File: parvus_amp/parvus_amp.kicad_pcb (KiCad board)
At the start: 2 copper layers, 86 x 60 mm, 43 parts, among them J1 input, J2 output, J3 powersupply, U1 LM3886

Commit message: WIP: Component placement.
Signed-off-by: Nenad Radulovic <nenad.b.radulovic@gmail.com>
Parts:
- removed R14: 7k5, Resistor_THT:R_Axial_DIN0207_L6.3mm_D2.5mm_P7.62mm_Horizontal
- added D4: BZX85C15, Diode_THT:D_DO-41_SOD81_P10.16mm_Horizontal, F.Cu at (115.4, 86.3)
- added J4: ctrl, Connector_PinHeader_2.54mm:PinHeader_1x04_P2.54mm_Vertical, F.Cu at (118.0, 90.1)
- C1: value 15p -> 2m2; footprint Capacitor_THT:C_Disc_D3.8mm_W2.6mm_P2.50mm -> Capacitor_THT:CP_Radial_D16.0mm_P7.50mm
- C10: value 2m2 -> 3p3; footprint Capacitor_THT:CP_Radial_D16.0mm_P7.50mm -> Capacitor_THT:C_Disc_D3.8mm_W2.6mm_P2.50mm
- C11: value 100n -> 47u; footprint Capacitor_THT:C_Rect_L7.0mm_W3.5mm_P5.00mm -> Capacitor_THT:CP_Radial_D6.3mm_P2.50mm
- C12: value 100u -> 10u; footprint Capacitor_THT:CP_Radial_D8.0mm_P3.50mm -> Capacitor_THT:CP_Radial_D5.0mm_P2.00mm
- C13: value 2m2 -> 100n; footprint Capacitor_THT:CP_Radial_D16.0mm_P7.50mm -> Capacitor_THT:C_Rect_L4.6mm_W3.0mm_P2.50mm_MKS02_FKP02
- C14: value 100n -> 10u; footprint Capacitor_THT:C_Rect_L7.0mm_W3.5mm_P5.00mm -> Capacitor_THT:CP_Radial_D5.0mm_P2.00mm
- C15: value 100u -> 100n; footprint Capacitor_THT:CP_Radial_D8.0mm_P3.50mm -> Capacitor_THT:C_Disc_D5.1mm_W3.2mm_P5.00mm
- C2: value 220n -> 2m2; footprint Capacitor_THT:C_Rect_L7.0mm_W3.5mm_P5.00mm -> Capacitor_THT:CP_Radial_D16.0mm_P7.50mm
- C3: value 100n -> 220n; footprint Capacitor_THT:C_Rect_L7.0mm_W3.5mm_P5.00mm -> Capacitor_THT:C_Rect_L4.6mm_W3.0mm_P2.50mm_MKS02_FKP02
- C4: value 470u -> 220n; footprint Capacitor_THT:CP_Radial_D8.0mm_P3.50mm -> Capacitor_THT:C_Rect_L4.6mm_W3.0mm_P2.50mm_MKS02_FKP02
- C5: value 220p -> 22n; footprint Capacitor_THT:C_Disc_D4.3mm_W1.9mm_P5.00mm -> Capacitor_THT:C_Rect_L4.6mm_W3.0mm_P2.50mm_MKS02_FKP02
- C6: value 1n -> 22n; footprint Capacitor_THT:C_Disc_D4.3mm_W1.9mm_P5.00mm -> Capacitor_THT:C_Rect_L4.6mm_W3.0mm_P2.50mm_MKS02_FKP02
- C7: value 470u -> 10u; footprint Capacitor_THT:CP_Radial_D8.0mm_P3.50mm -> Capacitor_THT:CP_Radial_D5.0mm_P2.00mm
- C8: value 15p -> 220u; footprint Capacitor_THT:C_Disc_D3.8mm_W2.6mm_P2.50mm -> Capacitor_THT:CP_Radial_D6.3mm_P2.50mm
- C9: value 100u -> 3p3; footprint Capacitor_THT:CP_Radial_D8.0mm_P3.50mm -> Capacitor_THT:C_Disc_D3.8mm_W2.6mm_P2.50mm
- D1, D2: footprint Diode_THT:D_DO-201AD_P12.70mm_Horizontal -> Diode_THT:D_DO-35_SOD27_P7.62mm_Horizontal
- D3: value BZX85C16 -> 1N4148
- J1: footprint TerminalBlock_Phoenix:TerminalBlock_Phoenix_PT-1,5-3-3.5-H_1x03_P3.50mm_Horizontal -> Connector_Phoenix_MC:PhoenixContact_MCV_1,5_3-G-3.5_1x03_P3.50mm_Vertical
- J2: value output -> power; footprint Connector_Phoenix_MC:PhoenixContact_MCV_1,5_2-G-3.5_1x02_P3.50mm_Vertical -> Connector_Phoenix_MC:PhoenixContact_MCV_1,5_3-G-3.81_1x03_P3.81mm_Vertical
- J3: value powersupply -> output; footprint Connector_Phoenix_MC:PhoenixContact_MCV_1,5_3-G-3.5_1x03_P3.50mm_Vertical -> Connector_Phoenix_MC:PhoenixContact_MCV_1,5_2-G-3.81_1x02_P3.81mm_Vertical
- L1: value 2u -> 4u; footprint Inductor_THT:L_Axial_L12.0mm_D5.0mm_P15.24mm_Horizontal_Fastron_MISC -> Inductor_THT:L_Axial_L20.3mm_D12.7mm_P7.62mm_Vertical_Vishay_IHA-201
- R1: value 1k6 -> 499; footprint Resistor_THT:R_Axial_DIN0207_L6.3mm_D2.5mm_P7.62mm_Horizontal -> Resistor_THT:R_Axial_DIN0207_L6.3mm_D2.5mm_P10.16mm_Horizontal
- R10: value 499 -> 10
- R11: value 7k5 -> 47k; footprint Resistor_THT:R_Axial_DIN0207_L6.3mm_D2.5mm_P10.16mm_Horizontal -> Resistor_THT:R_Axial_DIN0204_L3.6mm_D1.6mm_P5.08mm_Horizontal
- R12: value 10 -> 30k; footprint Resistor_THT:R_Axial_DIN0207_L6.3mm_D2.5mm_P10.16mm_Horizontal -> Resistor_THT:R_Axial_DIN0204_L3.6mm_D1.6mm_P5.08mm_Horizontal
- R13: value 1k6 -> 10k; footprint Resistor_THT:R_Axial_DIN0207_L6.3mm_D2.5mm_P7.62mm_Horizontal -> Resistor_THT:R_Axial_DIN0204_L3.6mm_D1.6mm_P5.08mm_Horizontal
- R2: value 4.7 -> 499; footprint Resistor_THT:R_Axial_DIN0411_L9.9mm_D3.6mm_P15.24mm_Horizontal -> Resistor_THT:R_Axial_DIN0207_L6.3mm_D2.5mm_P10.16mm_Horizontal
- R3: value 10 -> 499
- R4: value 100 -> 499; footprint Resistor_THT:R_Axial_DIN0207_L6.3mm_D2.5mm_P7.62mm_Horizontal -> Resistor_THT:R_Axial_DIN0207_L6.3mm_D2.5mm_P10.16mm_Horizontal
- R5: value 100 -> 12k; footprint Resistor_THT:R_Axial_DIN0207_L6.3mm_D2.5mm_P7.62mm_Horizontal -> Resistor_THT:R_Axial_DIN0207_L6.3mm_D2.5mm_P10.16mm_Horizontal
- R6: value 499 -> 12k
- R7: value 7k5 -> 3.9
- R8: value 100k -> 15k; footprint Resistor_THT:R_Axial_DIN0207_L6.3mm_D2.5mm_P7.62mm_Horizontal -> Resistor_THT:R_Axial_DIN0204_L3.6mm_D1.6mm_P5.08mm_Horizontal
- R9: value 4.7 -> 3.9; footprint Resistor_THT:R_Axial_DIN0411_L9.9mm_D3.6mm_P15.24mm_Horizontal -> Resistor_THT:R_Axial_DIN0207_L6.3mm_D2.5mm_P10.16mm_Horizontal
- U1: value LM3886 -> TDA7293; footprint Package_TO_SOT_THT:TO-220-11_P3.4x5.08mm_StaggerOdd_Lead4.85mm_Vertical -> Package_TO_SOT_THT:TO-220-15_P2.54x2.54mm_StaggerOdd_Lead4.58mm_Vertical
- moved C8 67.9 mm to (99.6, 68.5), turned to 180 degrees
- moved C7 65.1 mm to (99.6, 76.1), turned to 180 degrees
- moved J1 62.1 mm to (97.0, 94.5)
- moved R3 54.5 mm to (114.2, 67.9), turned to 180 degrees
- moved C13 53.2 mm to (144.6, 66.0), turned to 270 degrees
- moved D1 50.4 mm to (151.0, 55.8), turned to 270 degrees
- moved C15 49.1 mm to (159.2, 90.7), turned to 270 degrees
- moved R1 48.5 mm to (104.0, 80.6)
- moved R12 48.1 mm to (120.5, 72.9)
- moved D2 46.9 mm to (147.8, 63.4), turned to 90 degrees
- moved R4 46.5 mm to (114.2, 64.7), turned to 180 degrees
- moved R8 44.4 mm to (120.5, 78.0)
- moved R5 43.4 mm to (114.2, 74.2), turned to 180 degrees
- moved C3 41.5 mm to (129.4, 66.0)
- moved J3 40.4 mm to (150.4, 94.5)
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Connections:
- C1 pad 1: Net-(C1-Pad1) -> +pwvs
- C1 pad 2: Net-(C1-Pad2) -> GNDD
- C10 pad 1: VCC -> Net-(C10-Pad1)
- C10 pad 2: GNDPWR -> /preout
- C11 pad 1: VCC -> Net-(C11-Pad1)
- C11 pad 2: GNDPWR -> /preout
- C12 pad 1: VCC -> Net-(C12-Pad1)
- C12 pad 2: GNDPWR -> GNDD
- C13 pad 1: GNDPWR -> Net-(C13-Pad1)
- C13 pad 2: VEE -> GNDD
- C14 pad 1: GNDPWR -> Net-(C14-Pad1)
- C14 pad 2: VEE -> GNDD
- C15 pad 1: GNDPWR -> Net-(C15-Pad1)
- C15 pad 2: VEE -> GNDD
- C2 pad 1: Net-(C2-Pad1) -> GNDD
- C2 pad 2: Net-(C2-Pad2) -> -pwvs
- C3 pad 1: Net-(C3-Pad1) -> +pwvs
- C3 pad 2: Net-(C3-Pad2) -> GNDD
- C4 pad 1: Net-(C4-Pad1) -> GNDD
- C4 pad 2: Net-(C4-Pad2) -> -pwvs
- C5 pad 1: Net-(C5-Pad1) -> +pwvs
- C5 pad 2: Net-(C1-Pad1) -> GNDD
- C6 pad 1: Net-(C4-Pad2) -> GNDD
- C6 pad 2: Net-(C1-Pad1) -> -pwvs
- C7 pad 2: Net-(C1-Pad1) -> /input
- C8 pad 1: Net-(C2-Pad2) -> Net-(C8-Pad1)
- C8 pad 2: Net-(C8-Pad2) -> /sgnd
- C9 pad 1: GNDPWR -> /sgnd
- D1 pad 1: VCC -> +pwvs
- D1 pad 2: Net-(C2-Pad2) -> /preout
- D2 pad 1: Net-(C2-Pad2) -> /preout
- D2 pad 2: VEE -> -pwvs
- D3 pad 2: Net-(C9-Pad2) -> Net-(D3-Pad2)
- J1 pad 1: Net-(J1-Pad1) -> /input
- J1 pad 2: GNDPWR -> /sgnd
- J1 pad 3: Net-(C1-Pad1) -> GNDD
- J2 pad 1: GNDPWR -> +pwvs
- J2 pad 2: Net-(C3-Pad2) -> GNDD
- J3 pad 1: VCC -> /out
- J3 pad 2: GNDPWR -> GNDD
- L1 pad 1: Net-(C2-Pad2) -> /preout
- L1 pad 2: Net-(C3-Pad2) -> /out
- R1 pad 1: Net-(R1-Pad1) -> /sgnd
- R1 pad 2: Net-(C1-Pad2) -> /input
- R10 pad 1: Net-(R10-Pad1) -> /out
- R10 pad 2: Net-(C7-Pad1) -> Net-(C15-Pad1)
- R11 pad 1: Net-(C2-Pad2) -> Net-(D3-Pad1)
- R11 pad 2: Net-(R10-Pad1) -> Net-(D3-Pad2)
- R12 pad 1: Net-(C1-Pad1) -> Net-(D3-Pad1)
- R12 pad 2: GNDPWR -> Net-(C14-Pad1)
- R13 pad 1: Net-(R10-Pad1) -> GNDD
- R13 pad 2: Net-(C8-Pad2) -> Net-(D3-Pad1)
- R2 pad 1: GNDPWR -> GNDD
- R2 pad 2: Net-(C2-Pad1) -> /sgnd
- R3 pad 1: GNDPWR -> Net-(C9-Pad2)
- R3 pad 2: Net-(C3-Pad1) -> Net-(C7-Pad1)
- R4 pad 1: Net-(C5-Pad1) -> Net-(C10-Pad1)
- R4 pad 2: Net-(J1-Pad1) -> Net-(C8-Pad1)
- R5 pad 1: Net-(C4-Pad2) -> Net-(C9-Pad2)
- R5 pad 2: Net-(C5-Pad1) -> /sgnd
- R6 pad 1: Net-(R1-Pad1) -> Net-(C10-Pad1)
- R6 pad 2: Net-(C4-Pad1) -> /preout
- R7 pad 1: Net-(C1-Pad1) -> /preout
- R7 pad 2: Net-(R1-Pad1) -> Net-(C13-Pad1)
- R8 pad 1: Net-(J1-Pad1) -> Net-(D3-Pad2)
- R8 pad 2: Net-(C1-Pad1) -> Net-(C12-Pad1)
- R9 pad 1: Net-(C3-Pad2) -> /out
- R9 pad 2: Net-(C2-Pad2) -> /preout
- U1 pad 1: VCC -> GNDD
- U1 pad 10: Net-(R1-Pad1) -> Net-(C12-Pad1)
- U1 pad 2: (no net) -> Net-(C10-Pad1)
- U1 pad 3: Net-(C2-Pad2) -> Net-(C9-Pad2)
- U1 pad 4: VEE -> /sgnd
- U1 pad 5: VCC -> Net-(J4-Pad4)
- U1 pad 6: (no net) -> Net-(C11-Pad1)
- U1 pad 7: GNDPWR -> +pwvs
- U1 pad 8: Net-(D3-Pad1) -> -pwvs
- U1 pad 9: Net-(R10-Pad1) -> Net-(C14-Pad1)
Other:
- board size 86 x 60 mm -> 70 x 54.9 mm

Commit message: WIP: Routing components
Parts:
- removed the C11 at (140.8, 58.3)
- removed the C13 at (144.6, 66.0)
- removed the C15 at (159.2, 90.7)
- removed the C2 at (135.1, 78.7)
- removed C3: 220n, Capacitor_THT:C_Rect_L4.6mm_W3.0mm_P2.50mm_MKS02_FKP02
- removed the C7 at (99.6, 76.1)
- removed the D1 at (151.0, 55.8)
- removed the J4 at (118.0, 90.1)
- removed the R10 at (149.1, 88.2)
- removed the R13 at (120.5, 75.5)
- removed R8: 15k, Resistor_THT:R_Axial_DIN0204_L3.6mm_D1.6mm_P5.08mm_Horizontal
- added C10: 100n, Capacitor_THT:C_Disc_D5.1mm_W3.2mm_P5.00mm, F.Cu at (104.0, 89.5)
- added C12: 220n, Capacitor_THT:C_Rect_L4.6mm_W3.0mm_P2.50mm_MKS02_FKP02, F.Cu at (129.4, 66.0)
- added C14: 2m2, Capacitor_THT:CP_Radial_D16.0mm_P7.50mm, F.Cu at (133.3, 78.8)
- added C4: 47u, Capacitor_THT:CP_Radial_D6.3mm_P2.50mm, F.Cu at (143.0, 57.4)
- added C5: 220p, Capacitor_THT:C_Disc_D3.8mm_W2.6mm_P2.50mm, F.Cu at (114.2, 75.6)
- added C6: 3u3, Capacitor_THT:CP_Radial_D5.0mm_P2.00mm, F.Cu at (107.2, 72.4)
- added D3: 1N5404, Diode_THT:D_DO-201AD_P12.70mm_Horizontal, F.Cu at (158.5, 66.0)
- added J2: input, Connector_Phoenix_MC:PhoenixContact_MCV_1,5_3-G-3.5_1x03_P3.50mm_Vertical, F.Cu at (97.7, 80.6)
- added R14: 10, Resistor_THT:R_Axial_DIN0207_L6.3mm_D2.5mm_P10.16mm_Horizontal, F.Cu at (114.2, 93.3)
- added R4: 10k, Resistor_THT:R_Axial_DIN0207_L6.3mm_D2.5mm_P10.16mm_Horizontal, F.Cu at (127.5, 85.7)
- added R7: 12k, Resistor_THT:R_Axial_DIN0207_L6.3mm_D2.5mm_P10.16mm_Horizontal, F.Cu at (114.2, 81.9)
- C7: renamed from C8; value 220u -> 470u
- C9: value 3p3 -> 100n; footprint Capacitor_THT:C_Disc_D3.8mm_W2.6mm_P2.50mm -> Capacitor_THT:C_Rect_L4.6mm_W3.0mm_P2.50mm_MKS02_FKP02
- D2: value 1N5404 -> BZX79C15
- D4: value BZX85C15 -> 1N5404; footprint Diode_THT:D_DO-41_SOD81_P10.16mm_Horizontal -> Diode_THT:D_DO-201AD_P12.70mm_Horizontal
- J1: value input -> ctrl; footprint Connector_Phoenix_MC:PhoenixContact_MCV_1,5_3-G-3.5_1x03_P3.50mm_Vertical -> Connector_PinHeader_2.54mm:PinHeader_1x04_P2.54mm_Vertical
- R1: value 499 -> 15k; footprint Resistor_THT:R_Axial_DIN0207_L6.3mm_D2.5mm_P10.16mm_Horizontal -> Resistor_THT:R_Axial_DIN0204_L3.6mm_D1.6mm_P7.62mm_Horizontal
- R11: value 47k -> 10; footprint Resistor_THT:R_Axial_DIN0204_L3.6mm_D1.6mm_P5.08mm_Horizontal -> Resistor_THT:R_Axial_DIN0207_L6.3mm_D2.5mm_P10.16mm_Horizontal
- R12: value 30k -> 12k; footprint Resistor_THT:R_Axial_DIN0204_L3.6mm_D1.6mm_P5.08mm_Horizontal -> Resistor_THT:R_Axial_DIN0207_L6.3mm_D2.5mm_P10.16mm_Horizontal
- R2: value 499 -> 47k; footprint Resistor_THT:R_Axial_DIN0207_L6.3mm_D2.5mm_P10.16mm_Horizontal -> Resistor_THT:R_Axial_DIN0204_L3.6mm_D1.6mm_P7.62mm_Horizontal
- R3: value 499 -> 30k; footprint Resistor_THT:R_Axial_DIN0207_L6.3mm_D2.5mm_P10.16mm_Horizontal -> Resistor_THT:R_Axial_DIN0204_L3.6mm_D1.6mm_P7.62mm_Horizontal
- R6: value 12k -> 100
- moved LOGO1 78.9 mm to (137.0, 104.1)
- moved J3 44.7 mm to (105.9, 99.7)
- moved D4 38.2 mm to (152.9, 78.7), turned to 90 degrees
- moved C9 33.1 mm to (144.6, 68.6), turned to 90 degrees
- moved D2 29.8 mm to (125.0, 82.5), turned to 180 degrees
- moved R11 22.1 mm to (104.0, 85.1), turned to 0 degrees
- moved LOGO2 22.0 mm to (148.5, 102.4)
- moved J1 20.9 mm to (117.3, 89.5), turned to 90 degrees
- moved R6 20.4 mm to (114.2, 78.7)
- moved R12 15.9 mm to (114.2, 58.4), turned to 180 degrees
- moved R1 14.5 mm to (117.3, 74.9)
- moved L1 13.4 mm to (154.8, 87.6), turned to 180 degrees
- moved R5 11.9 mm to (104.0, 67.9), turned to 0 degrees
- moved R9 11.0 mm to (147.2, 95.9)
- moved R13 10.8 mm to (148.5, 66.0), turned to 270 degrees
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- renumbered C12 to C1, C1 to C11, C5 to C13, C4 to C15, C6 to C16, C14 to C2, C10 to C8, D3 to D1, J2 to J4, MK3 to MK2, MK2 to MK3, R4 to R10, R7 to R13
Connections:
- C1 pad 1: Net-(C12-Pad1) -> /mute
- C2 pad 1: Net-(C14-Pad1) -> /stby
- C8 pad 1: Net-(C10-Pad1) -> Net-(C8-Pad1)
- C9 pad 1: /sgnd -> Net-(C9-Pad1)
- C9 pad 2: Net-(C9-Pad2) -> GNDD
- D1 pad 1: Net-(D3-Pad1) -> Net-(D1-Pad1)
- D1 pad 2: Net-(D3-Pad2) -> Net-(D1-Pad2)
- D2 pad 1: /preout -> +pwvs
- D2 pad 2: -pwvs -> Net-(D2-Pad2)
- D4 pad 1: Net-(D4-Pad1) -> /preout
- D4 pad 2: Net-(D3-Pad1) -> -pwvs
- J1 pad 1: /input -> Net-(D2-Pad2)
- J1 pad 2: /sgnd -> Net-(D1-Pad1)
- J3 pad 1: /out -> GNDD
- J3 pad 2: GNDD -> /out
- R1 pad 1: /sgnd -> Net-(D1-Pad2)
- R1 pad 2: /input -> /mute
- R10 pad 1: Net-(C10-Pad1) -> Net-(C8-Pad1)
- R11 pad 1: Net-(D3-Pad1) -> /sgnd
- R11 pad 2: Net-(D3-Pad2) -> GNDD
- R12 pad 1: Net-(D3-Pad1) -> Net-(C8-Pad1)
- R12 pad 2: Net-(C14-Pad1) -> /preout
- R13 pad 2: Net-(C13-Pad1) -> Net-(C9-Pad1)
- R2 pad 1: GNDD -> Net-(D1-Pad1)
- R2 pad 2: /sgnd -> Net-(D1-Pad2)
- R3 pad 1: Net-(C9-Pad2) -> Net-(D1-Pad1)
- R3 pad 2: Net-(C7-Pad1) (its old number) -> /stby
- R5 pad 1: Net-(C9-Pad2) -> /sgnd
- R5 pad 2: /sgnd -> Net-(C6-Pad1)
- R6 pad 1: Net-(C10-Pad1) -> Net-(C5-Pad1)
- R6 pad 2: /preout -> /input
- U1 pad 10: Net-(C12-Pad1) -> /mute
- U1 pad 2: Net-(C10-Pad1) -> Net-(C8-Pad1)
- U1 pad 3: Net-(C9-Pad2) -> Net-(C6-Pad1)
- U1 pad 5: Net-(J4-Pad4) -> Net-(J1-Pad4)
- U1 pad 9: Net-(C14-Pad1) -> /stby
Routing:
- net GNDD: track 0.00 -> 120.1 mm
- net /preout: track 0.00 -> 103.6 mm
- net /sgnd: track 0.00 -> 102.8 mm
- net /out: track 0.00 -> 64.0 mm
- net +pwvs: track 0.00 -> 57.8 mm, vias 0 -> 1
- net -pwvs: track 0.00 -> 48.1 mm
- net /mute: track 0.00 -> 33.7 mm
- net Net-(J1-Pad4): track 0.00 -> 29.3 mm
- net Net-(D1-Pad1): track 0.00 -> 25.0 mm
- net Net-(C6-Pad1): track 0.00 -> 22.9 mm
- net Net-(C4-Pad1): track 0.00 -> 19.9 mm
- net Net-(C5-Pad1): track 0.00 -> 12.5 mm
- net Net-(C8-Pad1): track 0.00 -> 12.1 mm
- net /stby: track 0.00 -> 10.5 mm
- net /input: track 0.00 -> 10.1 mm
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- added copper zone on B.Cu, net +pwvs
- added copper zone on B.Cu, net -pwvs
- added copper zone on F.Cu, net GNDD
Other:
- board size 70 x 54.9 mm -> 70 x 54 mm
- net class signal added: clearance 0.2, trace_width 1, via_dia 0.8, via_drill 0.4

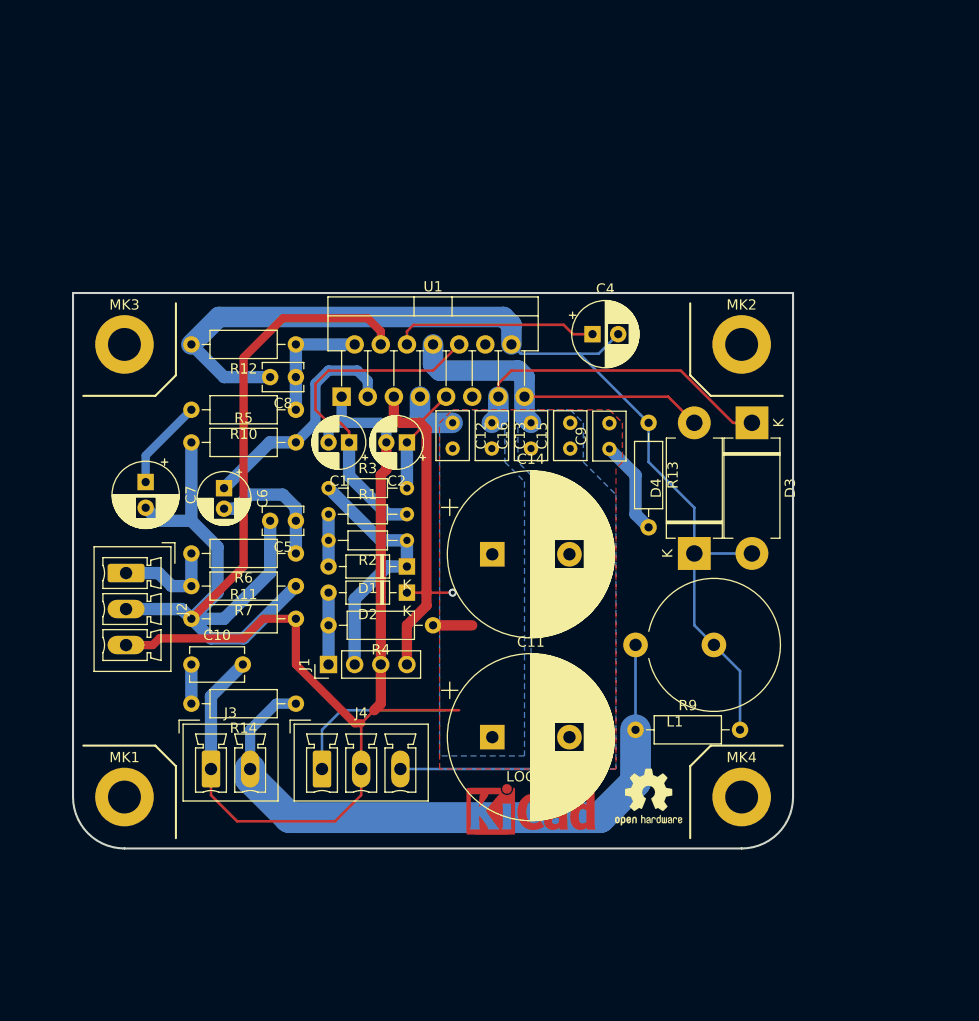
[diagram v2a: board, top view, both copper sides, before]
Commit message: WIP: Component pad editing.
Signed-off-by: Nenad Radulovic <nenad.b.radulovic@gmail.com>
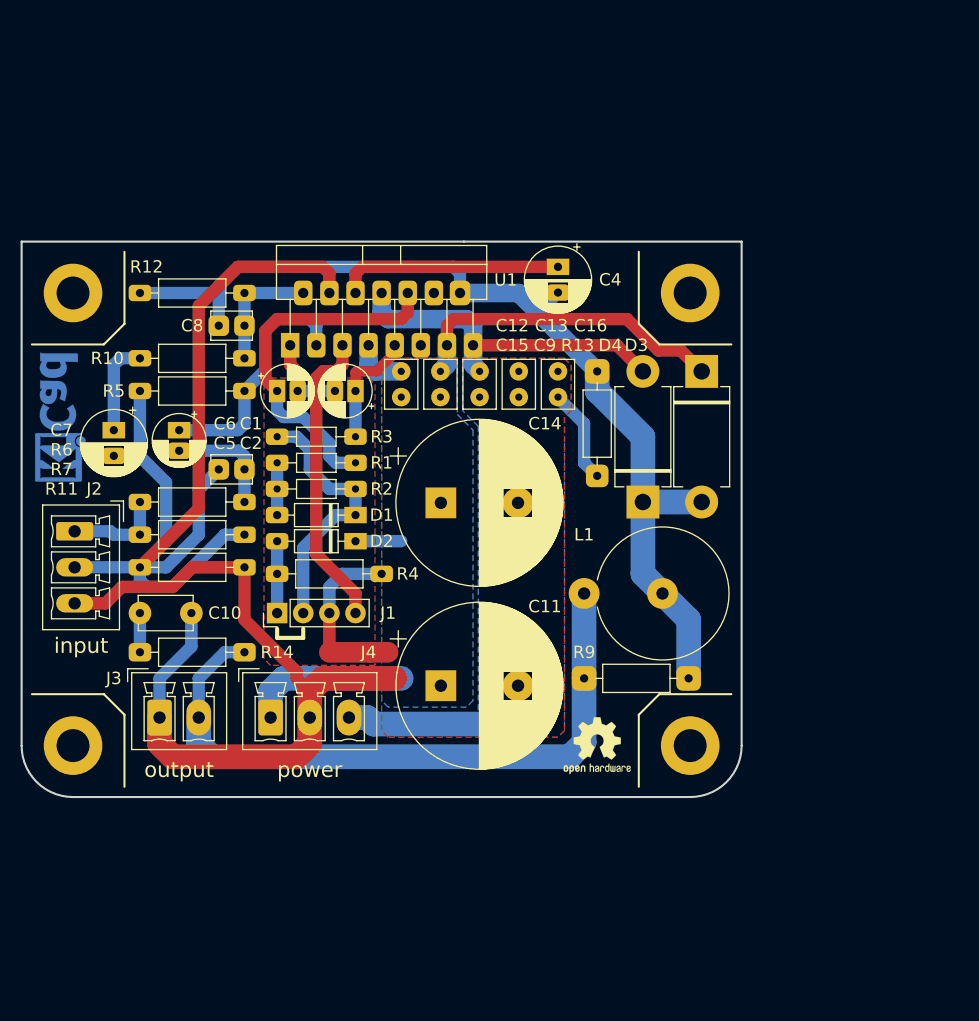
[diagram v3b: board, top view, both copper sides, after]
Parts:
- added NT1: Net-Tie_2, NetTie:NetTie-2_SMD_Pad2.0mm, F.Cu at (119.4, 88.3)
- LOGO1: moved to B.Cu
- moved LOGO1 60.3 mm to (90.8, 65.5), turned to 90 degrees
- moved C1 8.60 mm to (112.3, 62.9), turned to 0 degrees
- moved C4 7.35 mm to (139.6, 50.9), turned to 270 degrees
- moved C6 7.13 mm to (102.8, 66.8)
- moved C9 7.10 mm to (139.6, 63.5)
- moved C12 7.07 mm to (124.4, 61.0)
- moved C13 7.07 mm to (128.2, 61.0)
- moved C15 7.07 mm to (135.8, 63.5)
- moved C16 7.07 mm to (132.0, 63.5)
- moved R13 7.07 mm to (143.5, 61.0)
- moved C10 7.07 mm to (99.0, 84.5)
- moved C11 7.07 mm to (128.3, 91.6)
- moved C14 7.07 mm to (128.3, 73.8)
- moved C5 7.07 mm to (109.2, 70.6)
- moved C8 7.07 mm to (109.2, 56.6)
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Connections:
- C10 pad 2: GNDD -> GNDPWR
- C11 pad 2: GNDD -> GNDPWR
- C12 pad 2: GNDD -> GNDPWR
- C13 pad 2: GNDD -> GNDPWR
- C14 pad 1: GNDD -> GNDPWR
- C15 pad 1: GNDD -> GNDPWR
- C16 pad 1: GNDD -> GNDPWR
- C9 pad 2: GNDD -> GNDPWR
- J2 pad 3: GNDD -> GNDPWR
- J3 pad 1: GNDD -> GNDPWR
- J4 pad 2: GNDD -> GNDPWR
- R11 pad 2: GNDD -> GNDPWR
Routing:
- net GNDD: track 120.1 -> 20.3 mm
- net GNDPWR: track 0.00 -> 77.9 mm
- net /preout: track 103.6 -> 96.3 mm
- net /sgnd: track 102.8 -> 100.4 mm
- net Net-(C4-Pad1): track 19.9 -> 21.9 mm
- net Net-(C5-Pad1): track 12.5 -> 11.0 mm
- net /mute: track 33.7 -> 35.2 mm
- net Net-(C6-Pad1): track 22.9 -> 24.1 mm
- net /stby: track 10.5 -> 11.6 mm
- net Net-(D1-Pad1): track 25.0 -> 26.1 mm
- net /out: track 64.0 -> 64.9 mm
- net +pwvs: track 57.8 -> 57.3 mm, vias 1 -> 0
- added copper zone on F.Cu, net GNDPWR
